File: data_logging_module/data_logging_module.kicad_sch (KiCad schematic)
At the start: 4 parts

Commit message: Initial scheme
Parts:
- added J1, J2: Conn_01x11, Connector_PinHeader_2.54mm:PinHeader_1x11_P2.54mm_Vertical, symbol Connector_Generic:Conn_01x11
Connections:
- new net +3.3V: J1.3 (Pin_3)
- new net +3.3VA: J2.2 (Pin_2)
- new net BME280_SCB: J1.7 (Pin_7)
- new net BME280_SCK: J1.4 (Pin_4)
- new net BME280_SDI: J1.6 (Pin_6)
- new net BME280_SDO: J1.5 (Pin_5)
- new net DS18B20: J1.11 (Pin_11)
- new net GND: J1.1 (Pin_1), J2.1 (Pin_1)
- new net I2C_SCL: J1.8 (Pin_8)
- new net I2C_SDA: J1.9 (Pin_9)
- new net LDR: J1.10 (Pin_10)
- new net PCF8563_INT: J2.3 (Pin_3)
- new net SD_CARD_CD: J2.11 (Pin_11)
- new net SD_CARD_CLK/SCK: J2.4 (Pin_4)
- new net SD_CARD_CMD/MOSI: J2.5 (Pin_5)
- new net SD_CARD_CS/DAT3: J2.9 (Pin_9)
- new net SD_CARD_DAT0/MISO: J2.6 (Pin_6)
- new net SD_CARD_DAT1: J2.7 (Pin_7)
- new net SD_CARD_DAT2: J2.8 (Pin_8)
- new net SD_CARD_WP: J2.10 (Pin_10)
- new net VIN: J1.2 (Pin_2)

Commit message: BOM updates
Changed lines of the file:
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@@
 	(wire
 		(pts
-			(xy 90.17 101.6) (xy 90.17 78.74)
+			(xy 97.79 101.6) (xy 97.79 78.74)
 		)
 		(stroke
@@
 	(wire
 		(pts
-			(xy 86.36 78.74) (xy 86.36 101.6)
+			(xy 78.74 78.74) (xy 78.74 101.6)
 		)
 		(stroke
@@
 	(wire
 		(pts
-			(xy 90.17 78.74) (xy 110.49 78.74)
-		)
-		(stroke
-			(width 0)
-			(type default)
-		)
-	)
-	(wire
-		(pts
-			(xy 86.36 78.74) (xy 66.04 78.74)
+			(xy 97.79 78.74) (xy 110.49 78.74)
+		)
+		(stroke
+			(width 0)
+			(type default)
+		)
+	)
+	(wire
+		(pts
+			(xy 78.74 78.74) (xy 66.04 78.74)
 		)
 		(stroke
@@
 		(on_board yes)
 		(dnp no)
-		(fields_autoplaced yes)
 		(property "Reference" "J1"
-			(at 73.66 93.9799 0)
+			(at 69.85 80.264 0)
 			(effects
 				(font
@@
 		)
 		(property "Value" "Conn_01x11"
-			(at 73.66 96.5199 0)
+			(at 74.168 100.076 90)
 			(effects
 				(font
@@
 	(symbol
 		(lib_id "power:GND")
-		(at 86.36 101.6 0)
+		(at 78.74 101.6 0)
 		(unit 1)
 		(exclude_from_sim no)
@@
 		(fields_autoplaced yes)
 		(property "Reference" "#PWR046"
-			(at 86.36 107.95 0)
+			(at 78.74 107.95 0)
 			(effects
 				(font
@@
 		)
 		(property "Value" "GND"
-			(at 86.36 106.68 0)
+			(at 78.74 106.68 0)
 			(effects
 				(font
@@
 		)
 		(property "Footprint" ""
-			(at 86.36 101.6 0)
+			(at 78.74 101.6 0)
 			(effects
 				(font
@@
 		)
 		(property "Datasheet" ""
-			(at 86.36 101.6 0)
+			(at 78.74 101.6 0)
 			(effects
 				(font
@@
 		)
 		(property "Description" "Power symbol creates a global label with name \"GND\" , ground"
-			(at 86.36 101.6 0)
+			(at 78.74 101.6 0)
 			(effects
 				(font
@@
 		(dnp no)
 		(property "Reference" "J2"
-			(at 102.87 93.9799 0)
+			(at 106.426 80.01 0)
 			(effects
 				(font
@@
 		)
 		(property "Value" "Conn_01x11"
-			(at 102.87 96.5199 0)
+			(at 102.362 100.33 90)
 			(effects
 				(font
@@
 	(symbol
 		(lib_id "power:GND")
-		(at 90.17 101.6 0)
+		(at 97.79 101.6 0)
 		(unit 1)
 		(exclude_from_sim no)
@@
 		(fields_autoplaced yes)
 		(property "Reference" "#PWR047"
-			(at 90.17 107.95 0)
+			(at 97.79 107.95 0)
 			(effects
 				(font
@@
 		)
 		(property "Value" "GND"
-			(at 90.17 106.68 0)
+			(at 97.79 106.68 0)
 			(effects
 				(font
@@
 		)
 		(property "Footprint" ""
-			(at 90.17 101.6 0)
+			(at 97.79 101.6 0)
 			(effects
 				(font
@@
 		)
 		(property "Datasheet" ""
-			(at 90.17 101.6 0)
+			(at 97.79 101.6 0)
 			(effects
 				(font
@@
 		)
 		(property "Description" "Power symbol creates a global label with name \"GND\" , ground"
-			(at 90.17 101.6 0)
-			(effects
-				(font
+			(at 97.79 101.6 0)
+			(effects
+				(font

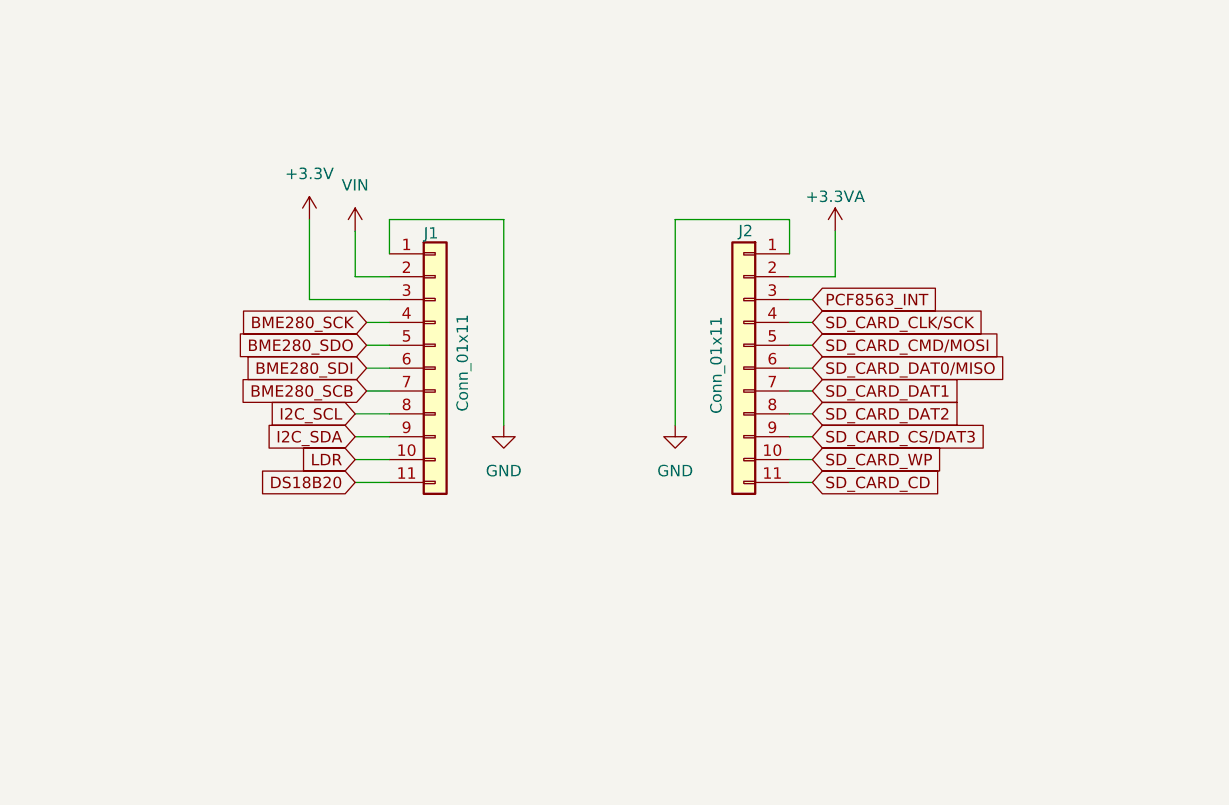
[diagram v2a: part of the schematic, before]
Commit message: PCB initial layout
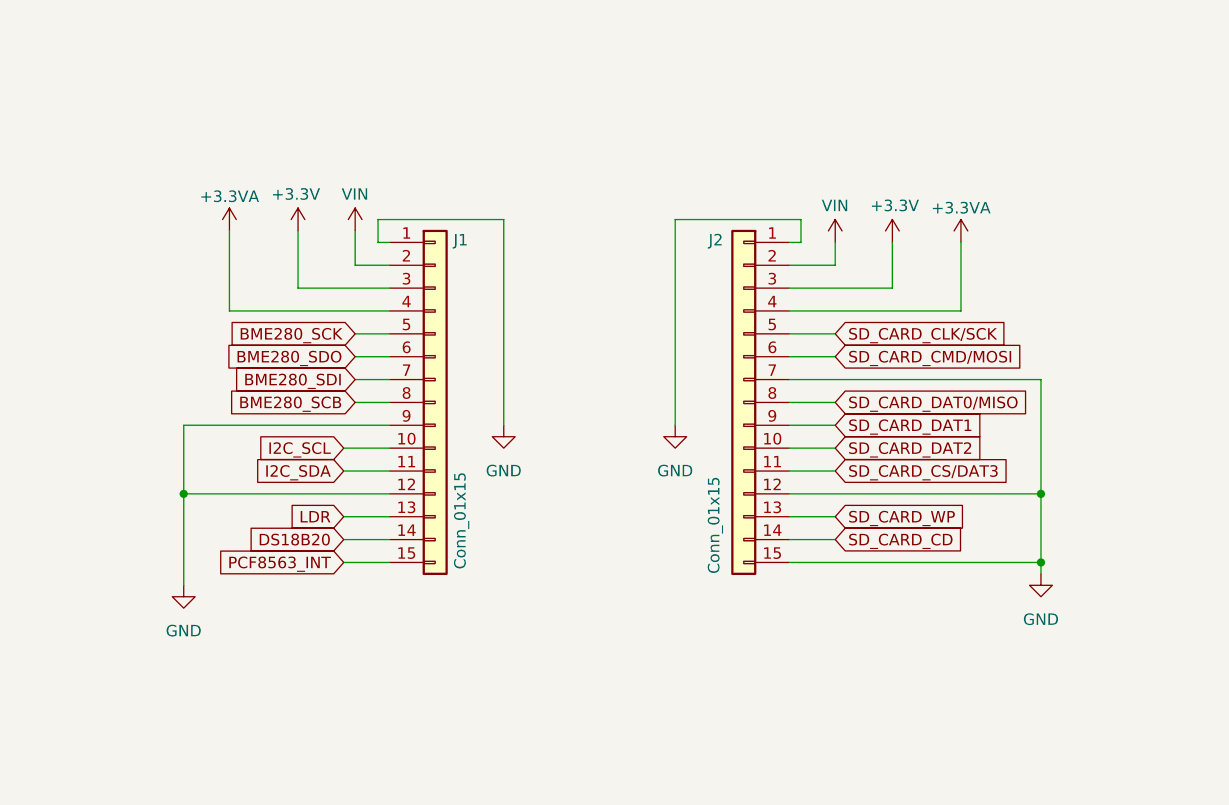
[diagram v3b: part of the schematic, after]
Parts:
- removed J1, J2: Conn_01x11, Connector_PinHeader_2.54mm:PinHeader_1x11_P2.54mm_Vertical, symbol Connector_Generic:Conn_01x11
- added J1, J2: Conn_01x15, Connector_PinSocket_2.54mm:PinSocket_1x15_P2.54mm_Vertical, symbol Connector_Generic:Conn_01x15
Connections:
- net +3.3V: now also J1.3 (Pin_3), J2.3 (Pin_3)
- net +3.3VA: now also J1.4 (Pin_4), J2.4 (Pin_4)
- net BME280_SCB: now also J1.8 (Pin_8)
- net BME280_SCK: now also J1.5 (Pin_5)
- net BME280_SDI: now also J1.7 (Pin_7)
- net BME280_SDO: now also J1.6 (Pin_6)
- net DS18B20: now also J1.14 (Pin_14)
- net GND: now also J1.1 (Pin_1), J1.12 (Pin_12), J1.9 (Pin_9), J2.1 (Pin_1), J2.12 (Pin_12), J2.15 (Pin_15), J2.7 (Pin_7)
- net I2C_SCL: now also J1.10 (Pin_10)
- net I2C_SDA: now also J1.11 (Pin_11)
- net LDR: now also J1.13 (Pin_13)
- net PCF8563_INT: now also J1.15 (Pin_15)
- net SD_CARD_CD: now also J2.14 (Pin_14)
- net SD_CARD_CLK/SCK: now also J2.5 (Pin_5)
- net SD_CARD_CMD/MOSI: now also J2.6 (Pin_6)
- net SD_CARD_CS/DAT3: now also J2.11 (Pin_11)
- net SD_CARD_DAT0/MISO: now also J2.8 (Pin_8)
- net SD_CARD_DAT1: now also J2.9 (Pin_9)
- net SD_CARD_DAT2: now also J2.10 (Pin_10)
- net SD_CARD_WP: now also J2.13 (Pin_13)
- net VIN: now also J1.2 (Pin_2), J2.2 (Pin_2)

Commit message: initial PCB
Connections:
- net DS18B20: now also J1.15 (Pin_15); no longer J1.14 (Pin_14)
- net LDR: now also J1.14 (Pin_14); no longer J1.13 (Pin_13)
- net PCF8563_INT: now also J1.13 (Pin_13); no longer J1.15 (Pin_15)

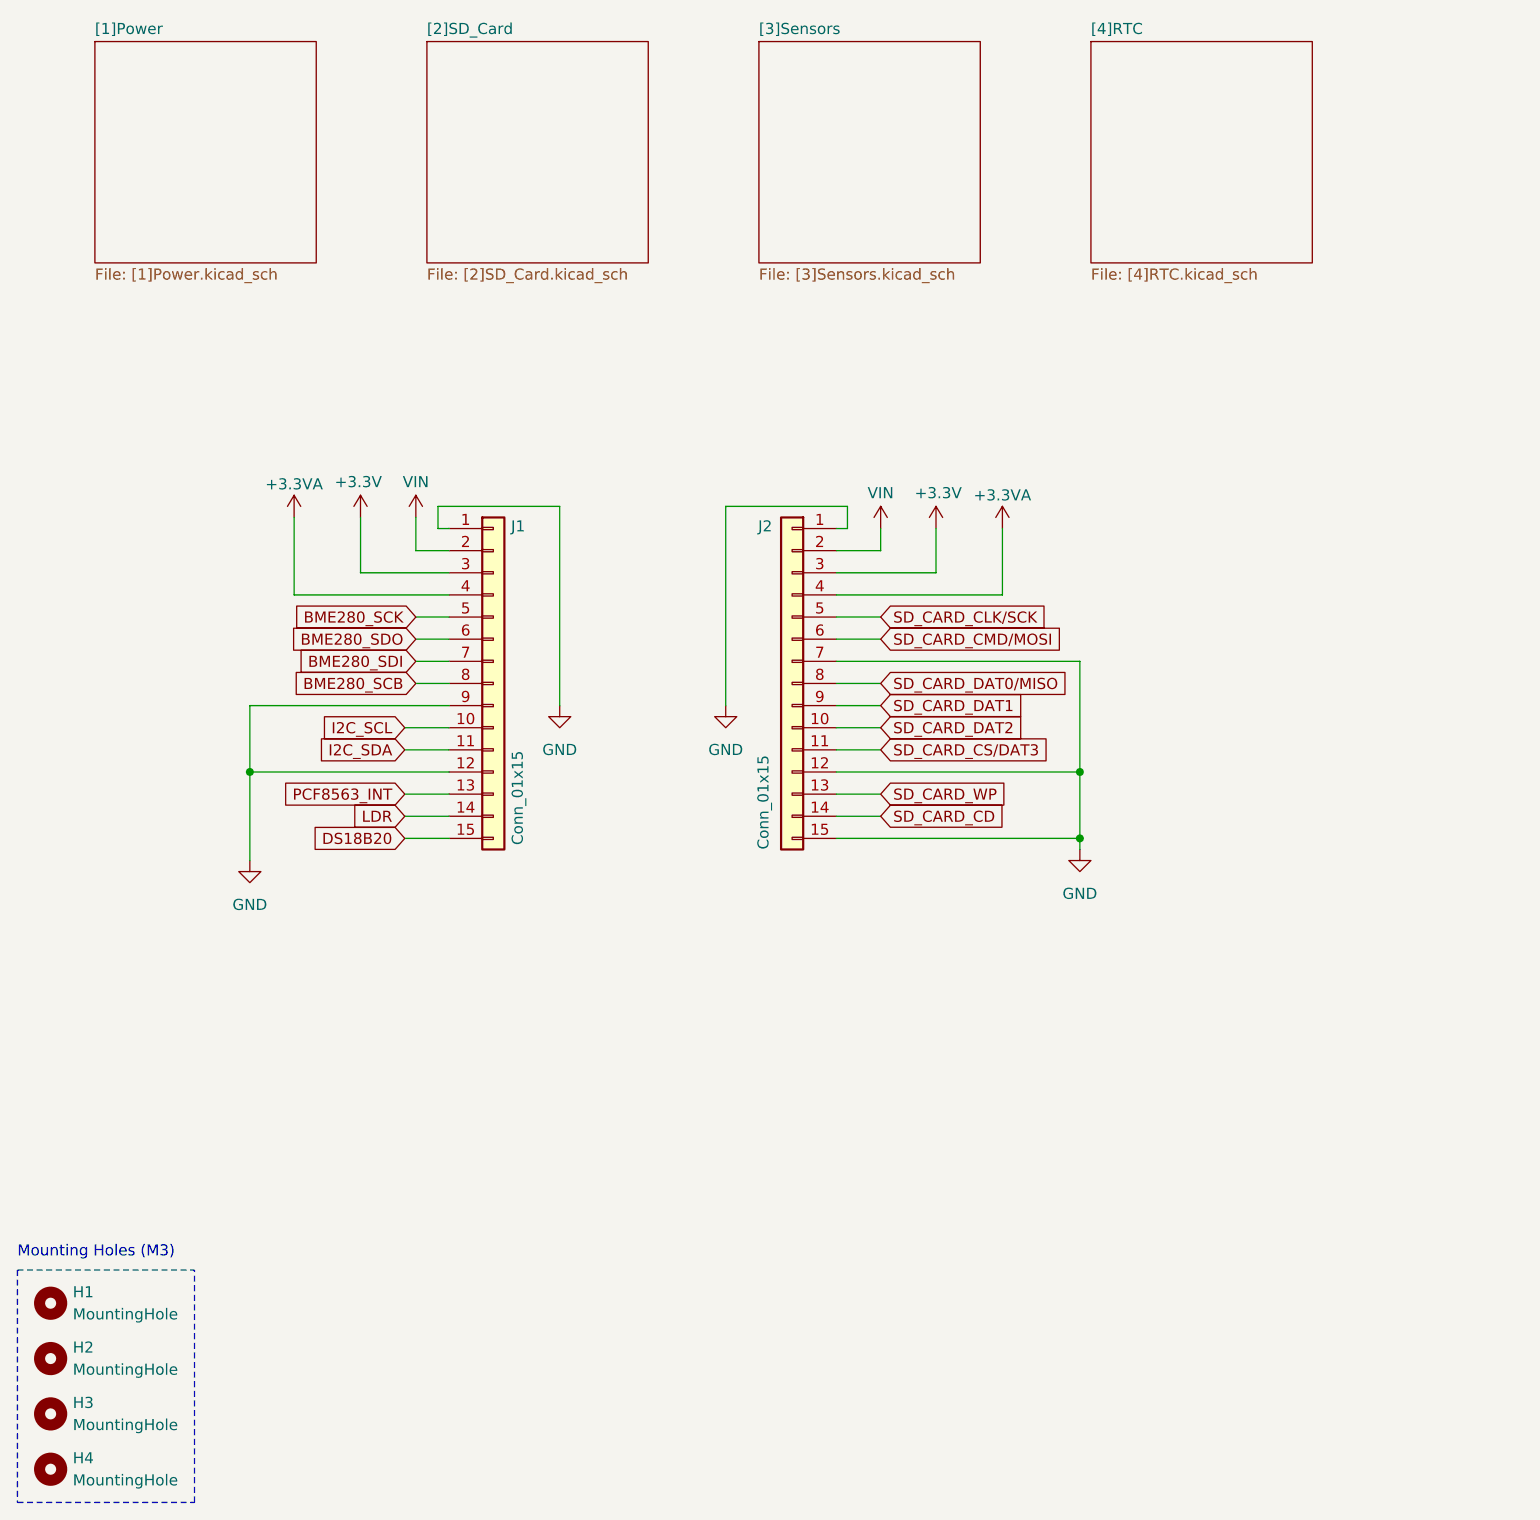
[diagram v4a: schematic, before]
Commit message: Add scheme plots
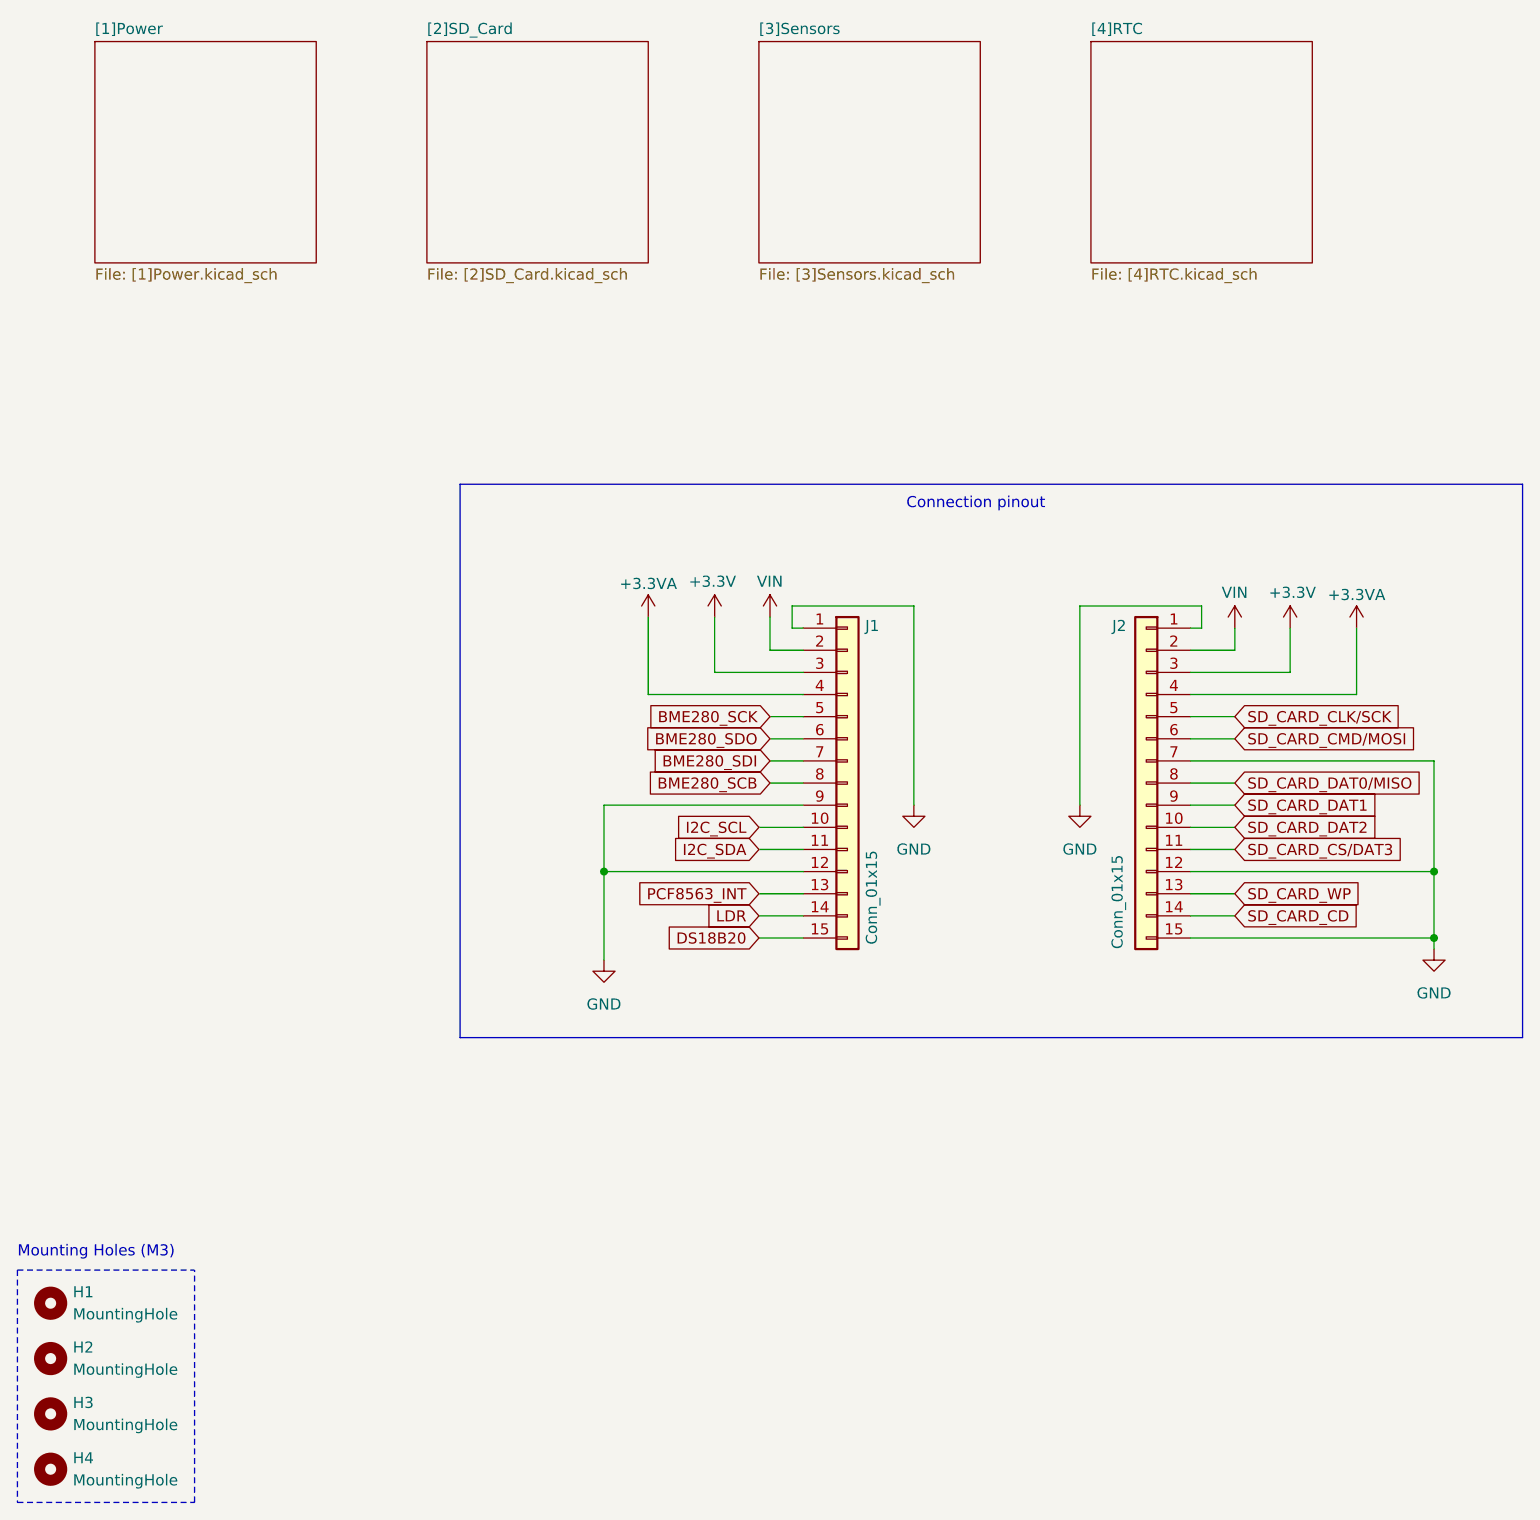
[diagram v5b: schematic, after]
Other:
- note added: "Connection pinout"
- moved on the sheet: J1, J2
